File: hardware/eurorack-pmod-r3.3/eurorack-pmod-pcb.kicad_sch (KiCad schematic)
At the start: 24 parts, among them Q1 2N7002E, U1 AK4619VN AUDIO CODEC, U2 TL074 OP AMP, U3 TL074 OP AMP, U4 PCA9557PW IO EXPANDER, U5 24AA025UIDT EEPROM, U6 CY8CMBR3108

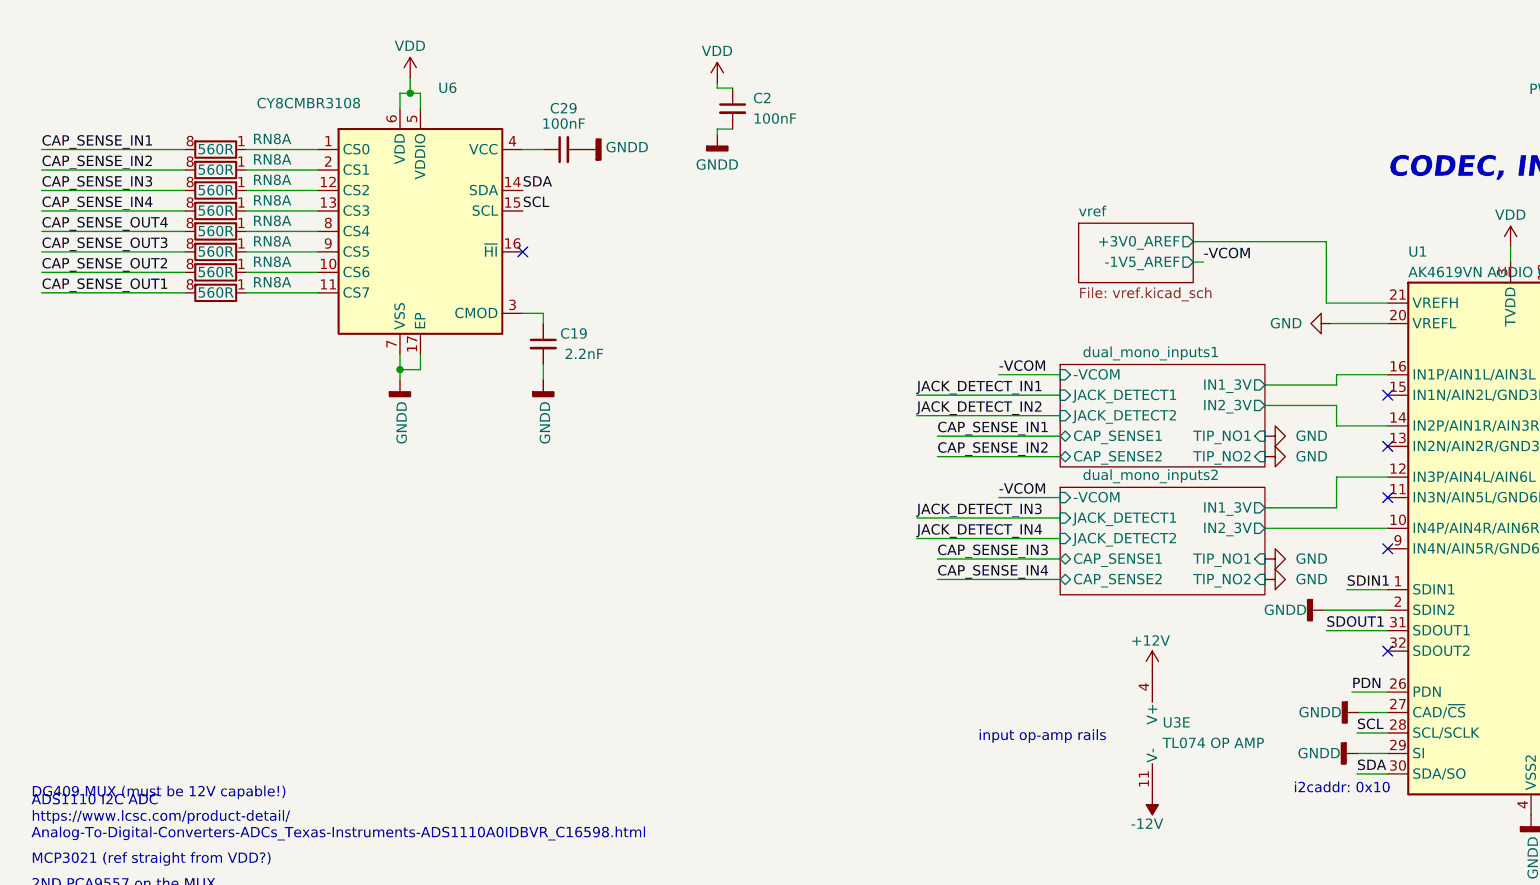
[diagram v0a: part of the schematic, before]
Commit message: - Swap stackup s/4/6     - Was: GND/SIG/SIG/GND     - Now: GND/VDD/SIG/SIG/GND/GND - Swap CY8CMBR3108 for CY8CMBR3116     - Touch indices do NOT match previous revision.     - TODO revise new pinout (XRES) - Combine GNDD and GNDA     - Remove inductors between planes     - Mounting hole connects to GNDD / GNDA - Clean up traces now moved to VDD plane - Add EMC 33R series on SDOUT1
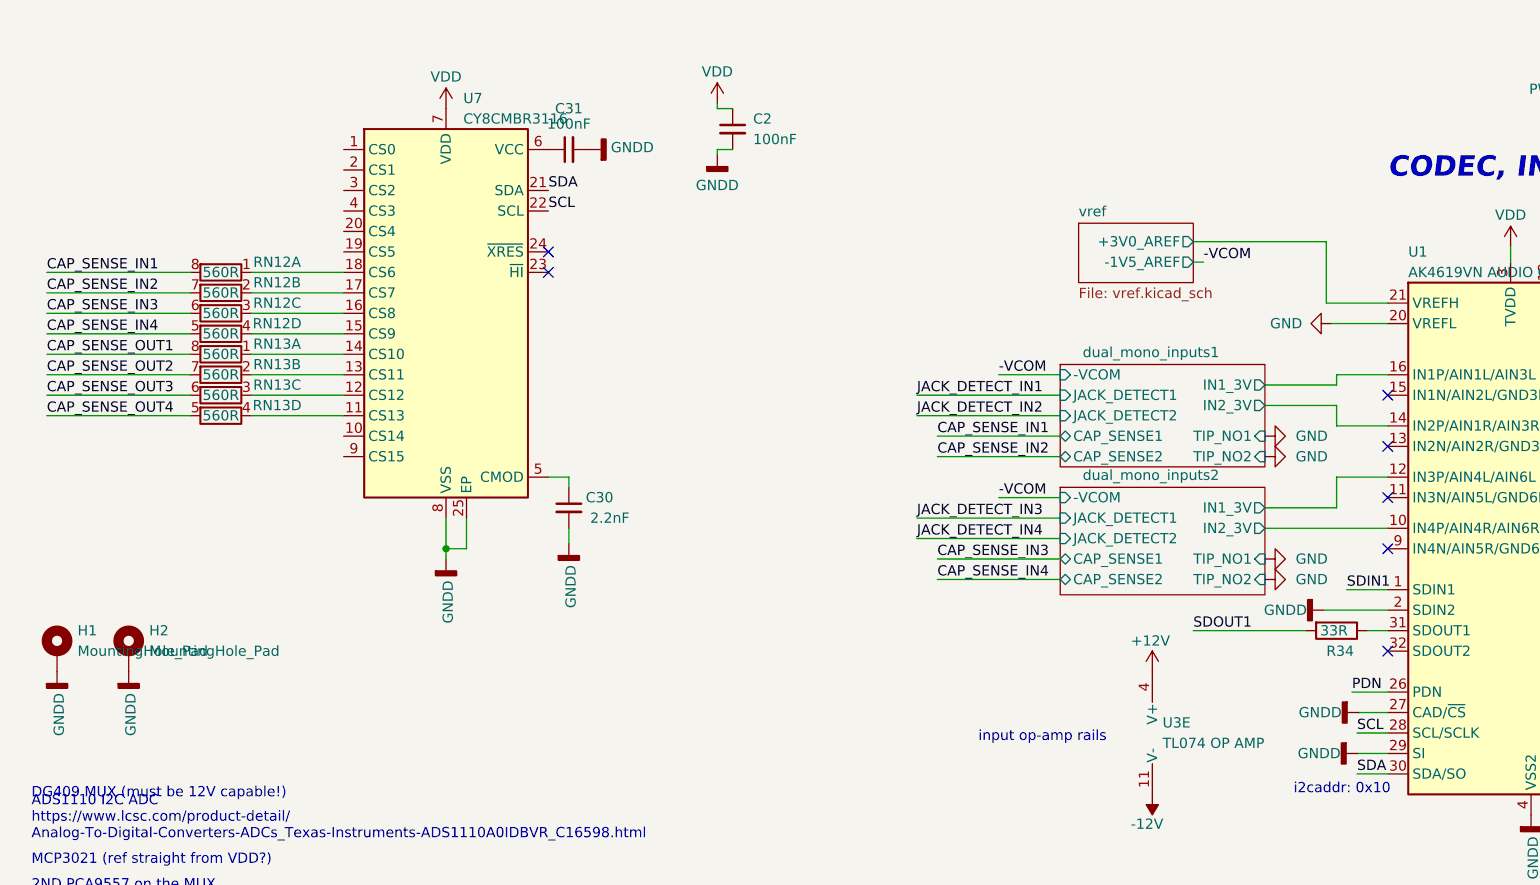
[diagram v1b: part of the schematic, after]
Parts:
- removed U6: CY8CMBR3108, Package_DFN_QFN:QFN-16-1EP_3x3mm_P0.5mm_EP1.75x1.75mm, symbol Sensor_Touch:CY8CMBR3108
- added H1, H2: MountingHole_Pad, symbol Mechanical:MountingHole_Pad
- added R34: 33R, Resistor_SMD:R_0402_1005Metric, symbol Device:R
- added U7: CY8CMBR3116, Package_DFN_QFN:QFN-24-1EP_4x4mm_P0.5mm_EP2.6x2.6mm, symbol Sensor_Touch:CY8CMBR3116
- renumbered C19 to C30, C29 to C31, RN8 to RN12, RN8 to RN13
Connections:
- net CAP_SENSE_IN2: now also RN12.7 (R2.2); no longer RN12.8 (R1.2)
- net CAP_SENSE_IN3: now also RN12.6 (R3.2); no longer RN12.8 (R1.2)
- net CAP_SENSE_IN4: now also RN12.5 (R4.2); no longer RN12.8 (R1.2)
- net CAP_SENSE_OUT2: now also RN13.7 (R2.2); no longer RN13.8 (R1.2)
- net CAP_SENSE_OUT3: now also RN13.6 (R3.2); no longer RN13.8 (R1.2)
- net CAP_SENSE_OUT4: now also RN13.5 (R4.2); no longer RN13.8 (R1.2)
- net GNDD: now also H1.1, H2.1, U7.25 (EP), U7.8 (VSS)
- net SCL: now also U7.22 (SCL)
- net SDA: now also U7.21 (SDA)
- net SDOUT1: now also R34.2; no longer U1.31 (SDOUT1)
- net VDD: now also U7.7 (VDD)
- net at C31.1: now also U7.6 (VCC)
- net at RN12.1 (R1.1): now also U7.18 (CS6)
- net at RN13.1 (R1.1): now also U7.14 (CS10)
- net at C30.1: now also U7.5 (CMOD)
- new net: RN12.3 (R3.1), U7.16 (CS8)
- new net: RN12.2 (R2.1), U7.17 (CS7)
- new net: RN13.2 (R2.1), U7.13 (CS11)
- new net: RN13.4 (R4.1), U7.11 (CS13)
- new net: R34.1, U1.31 (SDOUT1)
- new net: RN13.3 (R3.1), U7.12 (CS12)
- new net: RN12.4 (R4.1), U7.15 (CS9)
- no-connect marks 6 -> 7
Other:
- moved on the sheet: C2, C30, C31, RN12A, RN12B, RN12C, RN12D, RN13A, RN13B, RN13C, RN13D

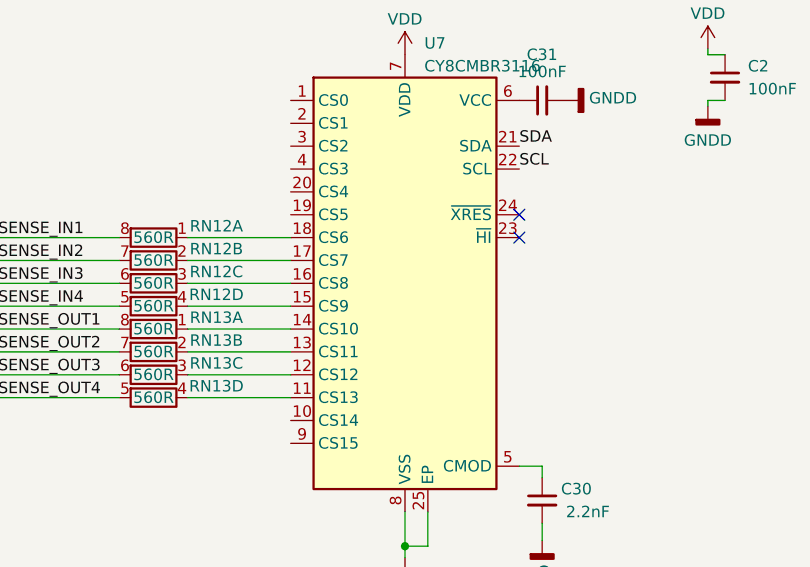
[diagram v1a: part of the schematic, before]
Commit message: - Add ceradiodes to audio ins/outs - Add low-capacitance TVS to touch channels (TODO footprint)
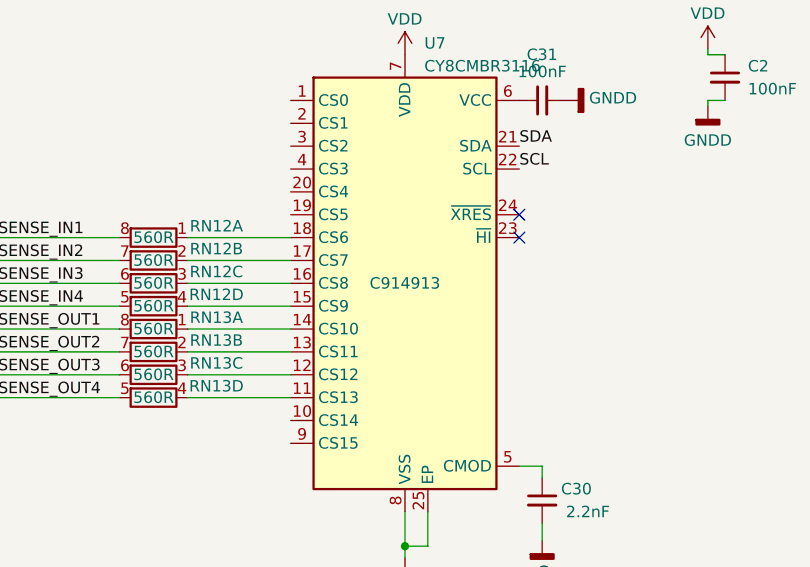
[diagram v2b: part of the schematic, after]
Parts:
- U7: lcsc# (none) -> C914913
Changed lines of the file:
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@@
+			)
+		)
+		(property "lcsc#" " C914913"
+			(at 68.58 49.53 0)
+			(effects
+				(font
+					(size 1.27 1.27)
+				)
 			)
 		)

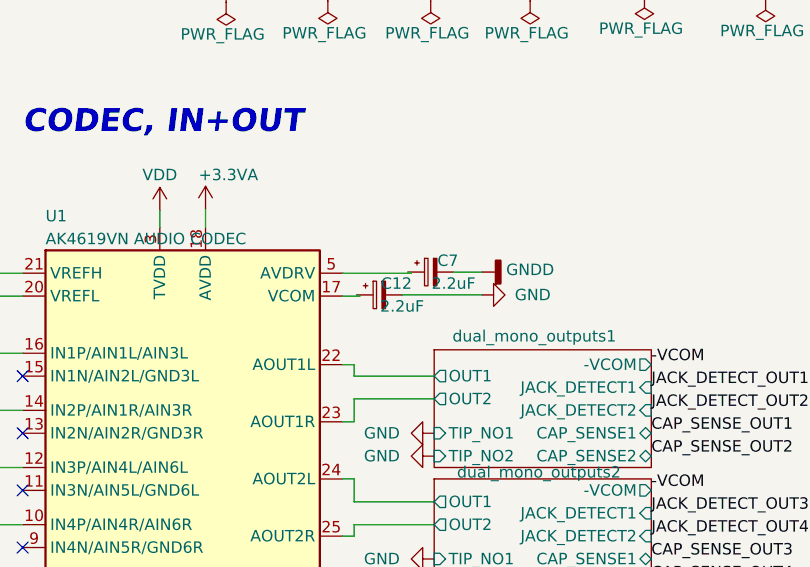
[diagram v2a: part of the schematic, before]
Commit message: - Swap all tantalums for ceramics
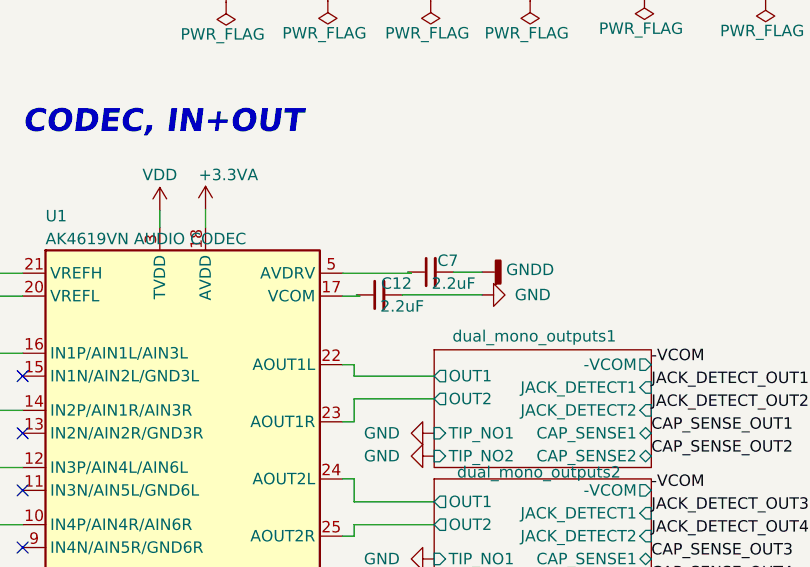
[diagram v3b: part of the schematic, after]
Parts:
- C12, C7: footprint Capacitor_Tantalum_SMD:CP_EIA-3216-10_Kemet-I -> Capacitor_SMD:C_1206_3216Metric; symbol Device:C_Polarized_Small -> Device:C_Small; lcsc# C2798035 -> C377799; mfg# T491A225K006AT -> (none)
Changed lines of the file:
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@@
 	)
 	(symbol
-		(lib_id "Device:C_Polarized_Small")
+		(lib_id "Device:C_Small")
 		(at 230.759 48.133 90)
 		(mirror x)
@@
 			)
 		)
-		(property "Footprint" "Capacitor_Tantalum_SMD:CP_EIA-3216-10_Kemet-I"
-			(at 230.759 48.133 0)
-			(effects
-				(font
-					(size 1.27 1.27)
-				)
-				(hide yes)
-			)
-		)
-		(property "Datasheet" ""
-			(at 230.759 48.133 0)
-			(effects
-				(font
-					(size 1.27 1.27)
-				)
-				(hide yes)
-			)
-		)
-		(property "Description" ""
-			(at 230.759 48.133 0)
-			(effects
-				(font
-					(size 1.27 1.27)
-				)
+		(property "Footprint" "Capacitor_SMD:C_1206_3216Metric"
+			(at 230.759 48.133 0)
+			(effects
+				(font
+					(size 1.27 1.27)
+				)
+				(hide yes)
+			)
+		)
+		(property "Datasheet" "~"
+			(at 230.759 48.133 0)
+			(effects
+				(font
+					(size 1.27 1.27)
+				)
+				(hide yes)
+			)
+		)
+		(property "Description" "Unpolarized capacitor, small symbol"
+			(at 230.759 48.133 0)
+			(effects
+				(font
+					(size 1.27 1.27)
+				)
+				(hide yes)
 			)
 		)
@@
 			)
 		)
-		(property "mfg#" "T491A225K006AT"
+		(property "mfg#" ""
 			(at 232.664 59.563 90)
 			(effects
@@
 			)
 		)
-		(property "lcsc#" "C2798035"
+		(property "lcsc#" "C377799"
 			(at 230.759 48.133 0)
 			(effects
@@
 	)
 	(symbol
-		(lib_id "Device:C_Polarized_Small")
+		(lib_id "Device:C_Small")
 		(at 225.044 50.673 90)
 		(mirror x)
@@
 			)
 		)
-		(property "Footprint" "Capacitor_Tantalum_SMD:CP_EIA-3216-10_Kemet-I"
-			(at 225.044 50.673 0)
-			(effects
-				(font
-					(size 1.27 1.27)
-				)
-				(hide yes)
-			)
-		)
-		(property "Datasheet" ""
-			(at 225.044 50.673 0)
-			(effects
-				(font
-					(size 1.27 1.27)
-				)
-				(hide yes)
-			)
-		)
-		(property "Description" ""
-			(at 225.044 50.673 0)
-			(effects
-				(font
-					(size 1.27 1.27)
-				)
+		(property "Footprint" "Capacitor_SMD:C_1206_3216Metric"
+			(at 225.044 50.673 0)
+			(effects
+				(font
+					(size 1.27 1.27)
+				)
+				(hide yes)
+			)
+		)
+		(property "Datasheet" "~"
+			(at 225.044 50.673 0)
+			(effects
+				(font
+					(size 1.27 1.27)
+				)
+				(hide yes)
+			)
+		)
+		(property "Description" "Unpolarized capacitor, small symbol"
+			(at 225.044 50.673 0)
+			(effects
+				(font
+					(size 1.27 1.27)
+				)
+				(hide yes)
 			)
 		)
@@
 			)
 		)
-		(property "mfg#" "T491A225K006AT"
+		(property "mfg#" ""
 			(at 226.949 62.103 90)
 			(effects
@@
 			)
 		)
-		(property "lcsc#" "C2798035"
-			(at 225.044 50.673 0)
-			(effects
+		(property "lcsc#" "C377799"
+			(at 225.044 50.673 0)
+			(effects

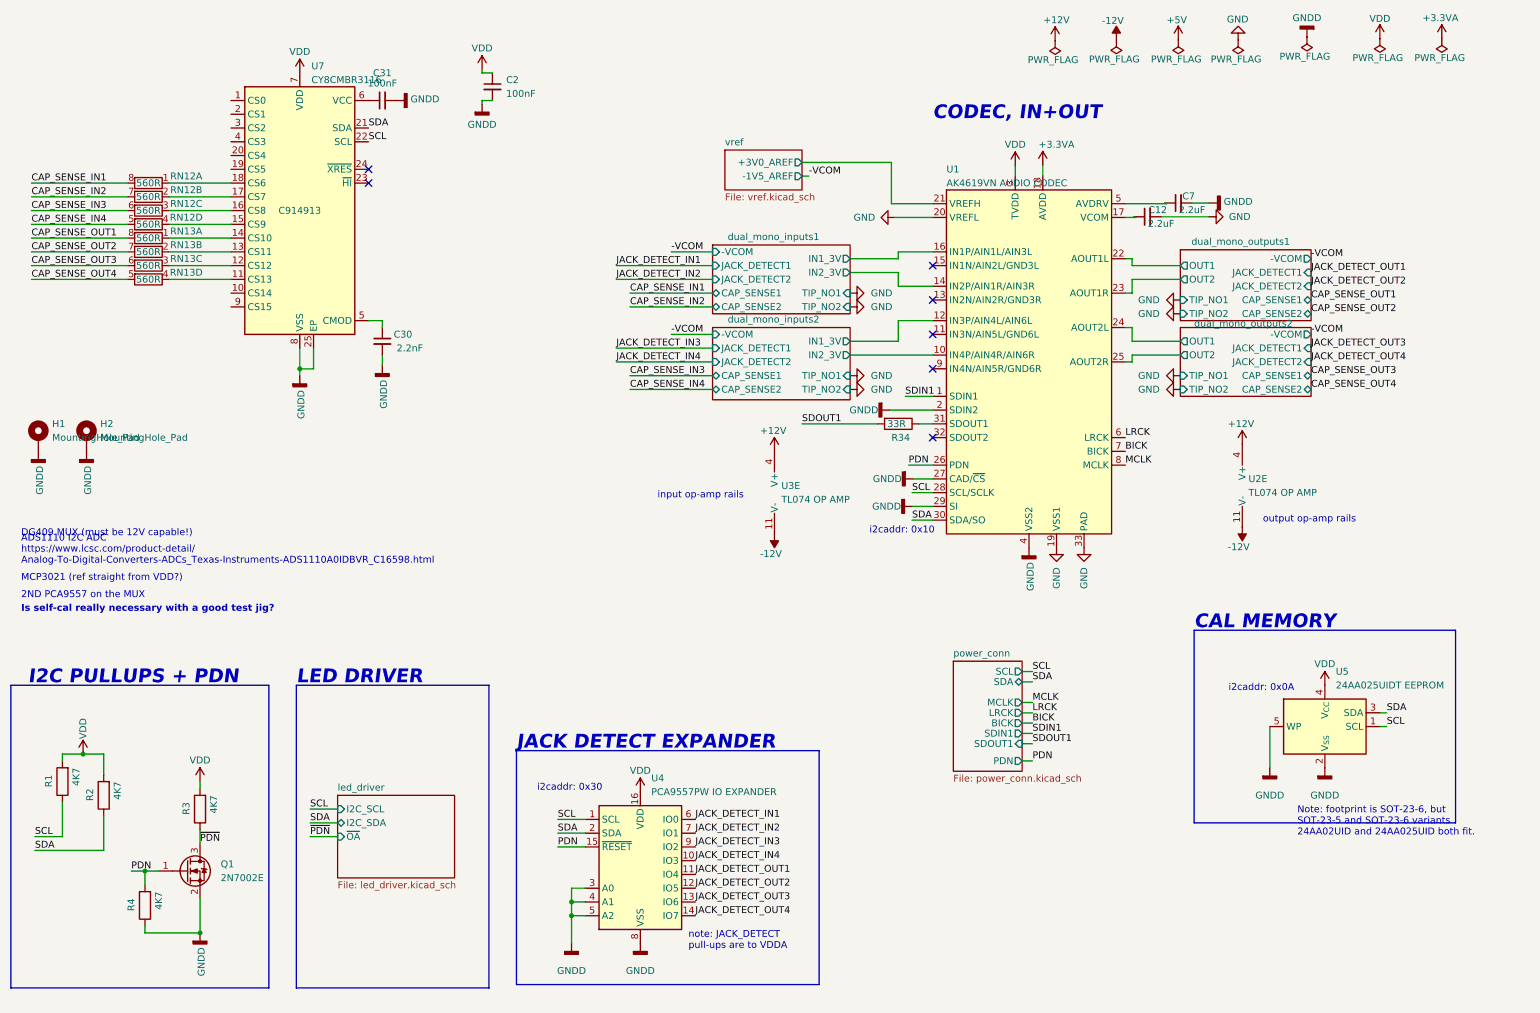
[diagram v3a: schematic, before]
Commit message: - touch: fix XRES on CS6 (!!) - mute: start on JFET output mute
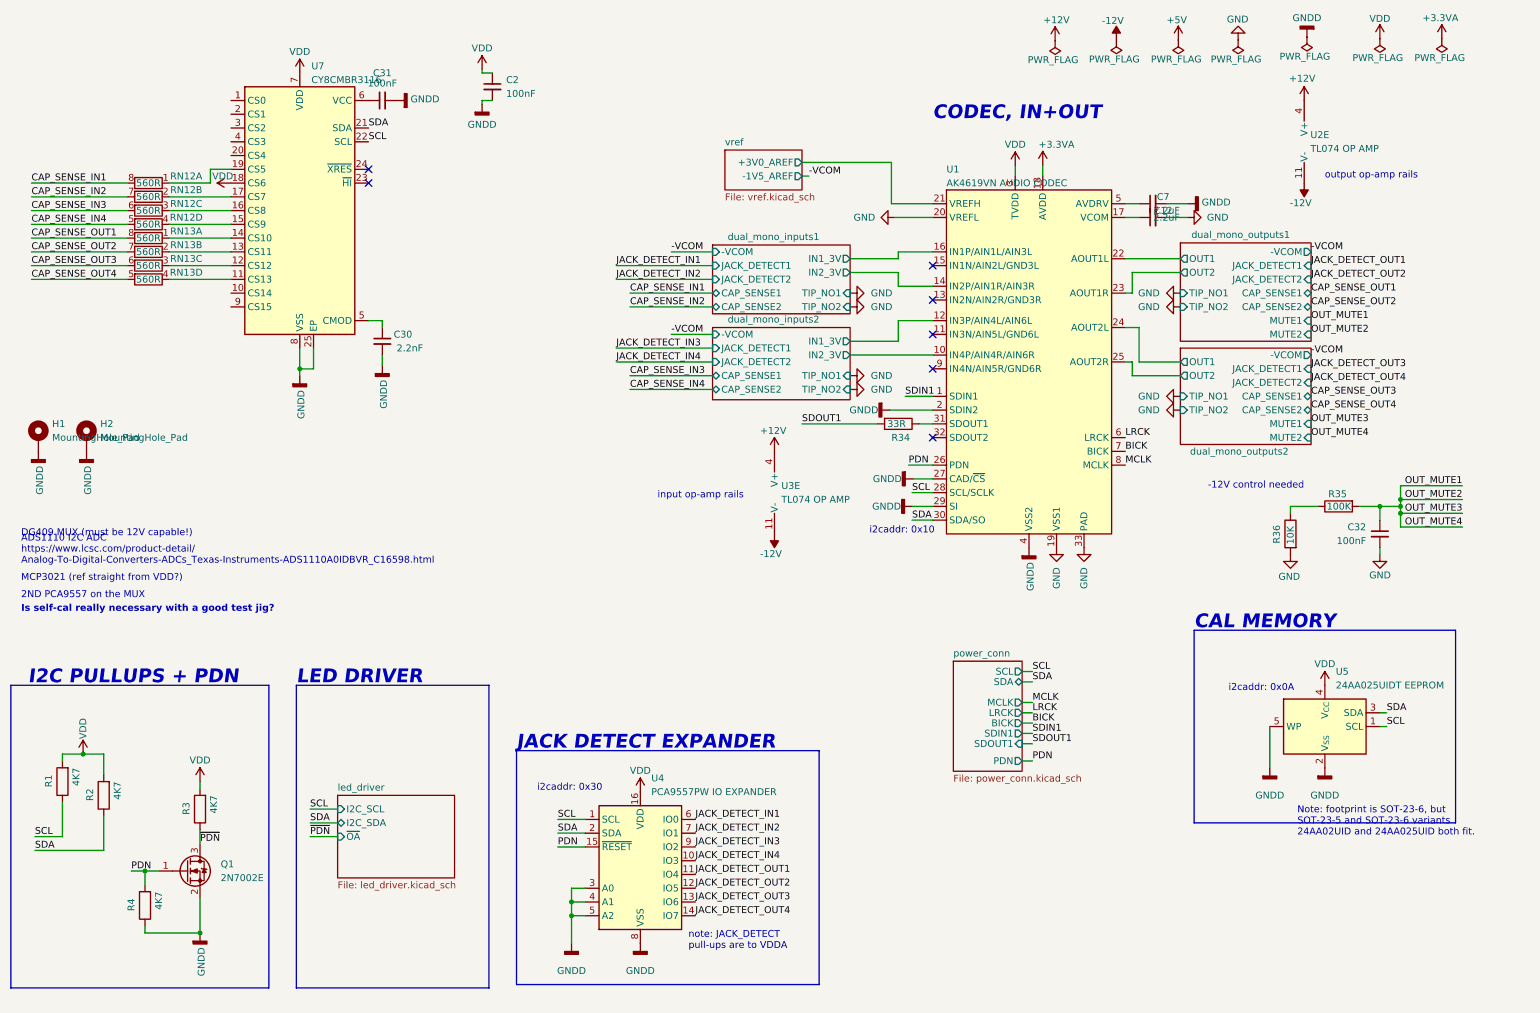
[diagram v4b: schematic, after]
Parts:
- added C32: 100nF, Capacitor_SMD:C_0603_1608Metric, symbol Device:C_Small
- added R35: 100K, Resistor_SMD:R_0402_1005Metric, symbol Device:R
- added R36: 10K, Resistor_SMD:R_0402_1005Metric, symbol Device:R
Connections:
- net GND: now also C32.2, R36.2
- net VDD: now also U7.18 (CS6)
- net at RN12.1 (R1.1): now also U7.19 (CS5); no longer U7.18 (CS6)
- new net: R35.1, R36.1
- new net OUT_MUTE1: C32.1, R35.2
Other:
- sheet dual_mono_outputs1 ports: added MUTE1, MUTE2; removed none
- sheet dual_mono_outputs2 ports: added MUTE1, MUTE2; removed none
- note added: "-12V control needed"
- moved on the sheet: C12, C7, U2E
